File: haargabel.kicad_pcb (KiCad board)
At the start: 4 copper layers, 140 x 50 mm, 84 parts, among them J1 SWD, J2 USB_B_Micro, J3 Conn_01x02, SW1 SW_Push, U1 ATSAML21E15B-MUT, U2 MCP73831-2-OT, U3 TPS79330-EP, U4 TPS22929D, U5 MPU-6050

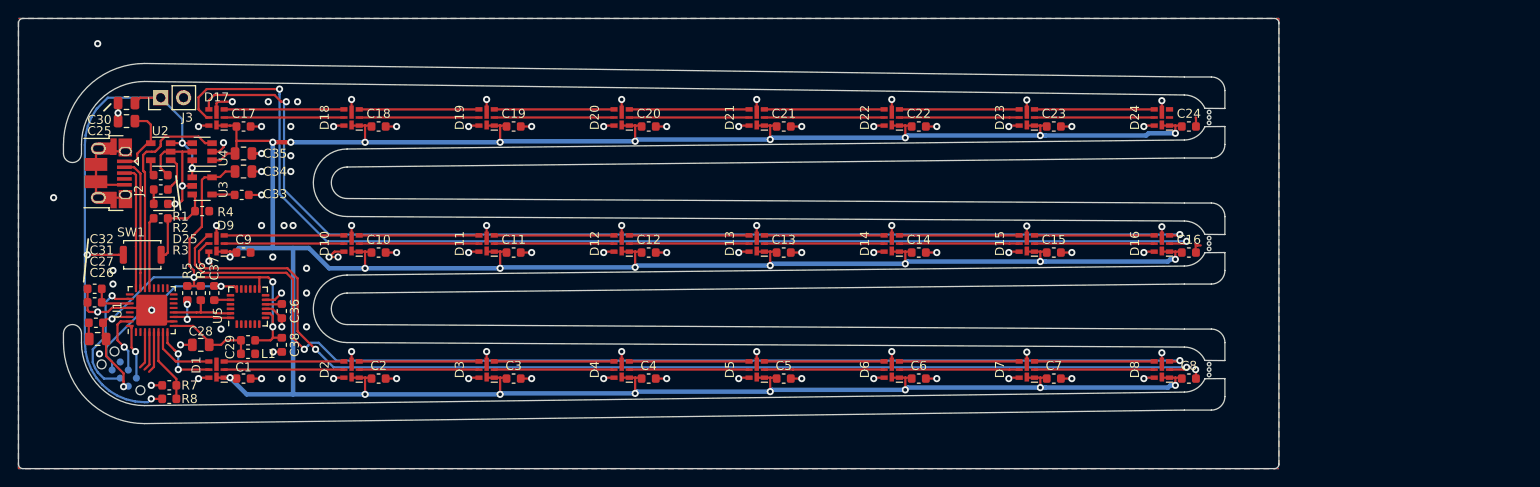
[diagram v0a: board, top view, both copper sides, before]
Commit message: Fix startup circuit
Use a zener-diode instead of just resistors.
This makes stuff much easier since it 'protects' the CPU from the high battery voltage.
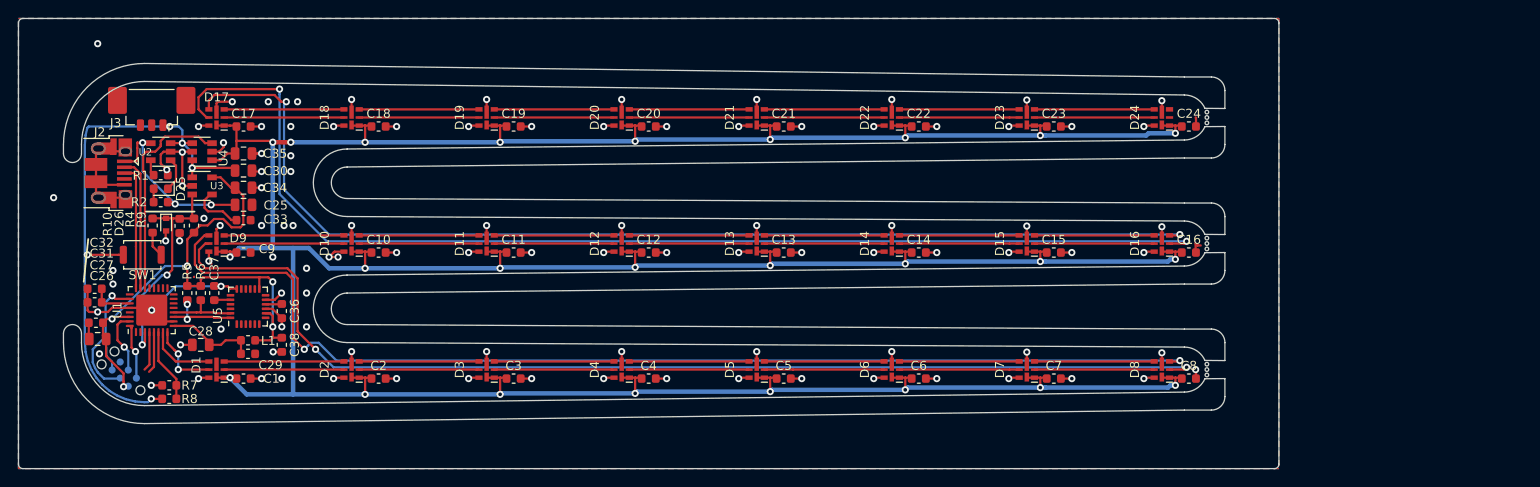
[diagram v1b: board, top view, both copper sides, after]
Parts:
- removed R3: 470R, Resistor_SMD:R_0603_1608Metric
- added D26: BZT52C2V7T-7, Diode_SMD:D_SOD-523, F.Cu at (119.4, 65.9)
- added R10: 270R, Resistor_SMD:R_0603_1608Metric, F.Cu at (117.9, 66.0)
- added R9: 270, Resistor_SMD:R_0603_1608Metric, F.Cu at (122.5, 66.0)
- J3: value Conn_01x02 -> Conn_01x03; footprint Connector_PinHeader_2.54mm:PinHeader_1x02_P2.54mm_Vertical -> Connector_Molex:Molex_PicoBlade_53398-0371_1x03-1MP_P1.25mm_Vertical
- R4: value 100k -> 1k
- moved C25 16.0 mm to (128.0, 63.7), turned to 0 degrees
- moved C30 15.0 mm to (128.0, 59.9), turned to 180 degrees
- moved R4 2.99 mm to (120.9, 66.0), turned to 270 degrees
- moved C33 2.81 mm to (128.0, 65.4)
- moved J3 2.06 mm to (117.8, 53.6), turned to 180 degrees
- moved C34 1.80 mm to (128.0, 61.8)
- moved D25 1.69 mm to (118.8, 61.9)
- moved R2 1.40 mm to (118.8, 63.4)
- moved H1 0.25 mm to (235.0, 68.0)
- moved H2 0.25 mm to (235.0, 82.0)
- moved H3 0.25 mm to (235.0, 54.0)
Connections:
- D25 pad 1: GND -> /STAT
- J3 pad 2: GND -> Net-(J3-Pad2)
- R2 pad 2: /STAT -> VBUS
- R4 pad 1: Net-(R3-Pad1) -> /EN
- SW1 pad 1: Net-(R3-Pad1) -> Net-(R10-Pad1)
- U1 pad 21: /PWR_ON -> Net-(U1-Pad21)
- U1 pad 3: Net-(U1-Pad3) -> /EN
- U3 pad 3: Net-(R3-Pad1) -> /EN
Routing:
- net /EN: track 0.00 -> 24.5 mm, vias 0 -> 2
- net VBUS: track 8.22 -> 21.1 mm, vias 0 -> 3
- net GND: track 198.2 -> 188.0 mm, vias 104 -> 107
- net Net-(R3-Pad1): track 9.98 -> 0.00 mm
- net /PWR_ON: track 7.95 -> 0.00 mm
- net +3V0: track 62.7 -> 67.0 mm
- net Net-(U1-Pad3): track 4.14 -> 0.00 mm
- net Net-(C33-Pad2): track 2.53 -> 6.06 mm
- net Net-(R10-Pad1): track 0.00 -> 2.86 mm
- net +BATT: track 67.5 -> 66.3 mm, vias 4 -> 5
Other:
- board text added: "r01"

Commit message: Remove the DIY-Panel, make it more pointy
The Fab will fuck up the routing anyway. Lets just hope they place the tabs somewhat reasonable.
The round ends were not pointy enough, fix them.
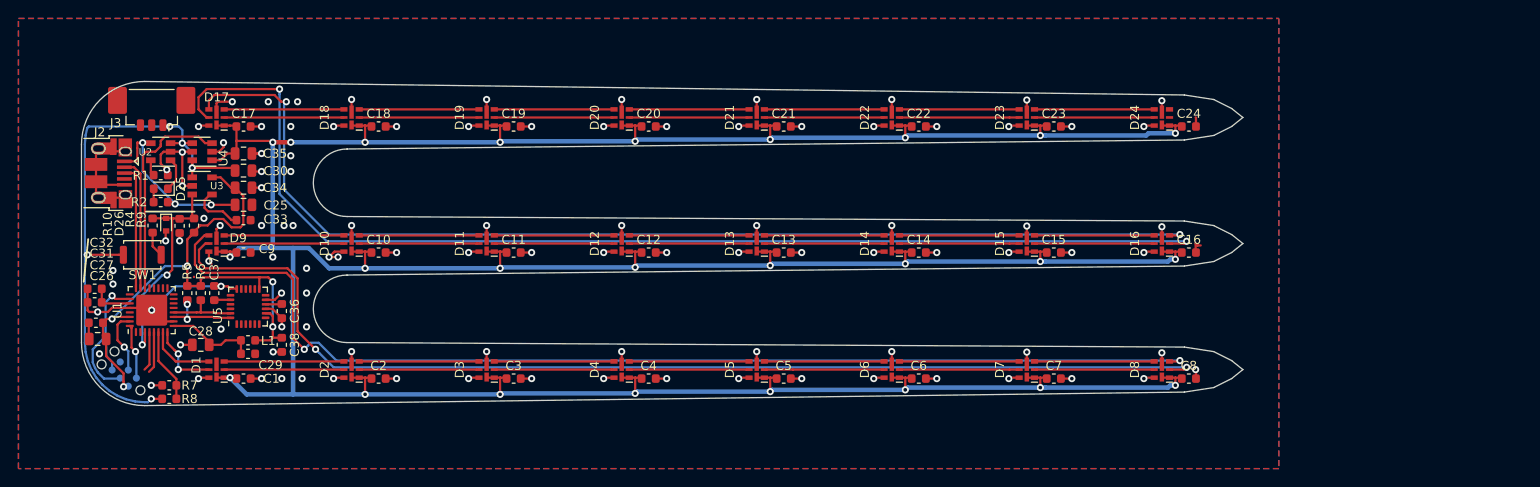
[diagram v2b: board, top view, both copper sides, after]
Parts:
- removed H1, H2, H3: MountingHole, MountingHole:Mousebite_0.4_0.6
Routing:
- net GND: track 188.0 -> 163.9 mm, vias 107 -> 105
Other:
- board size 140 x 50 mm -> 129 x 36 mm

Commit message: Make it longer
Add two more LEDs, making the whole thing 30mm longer
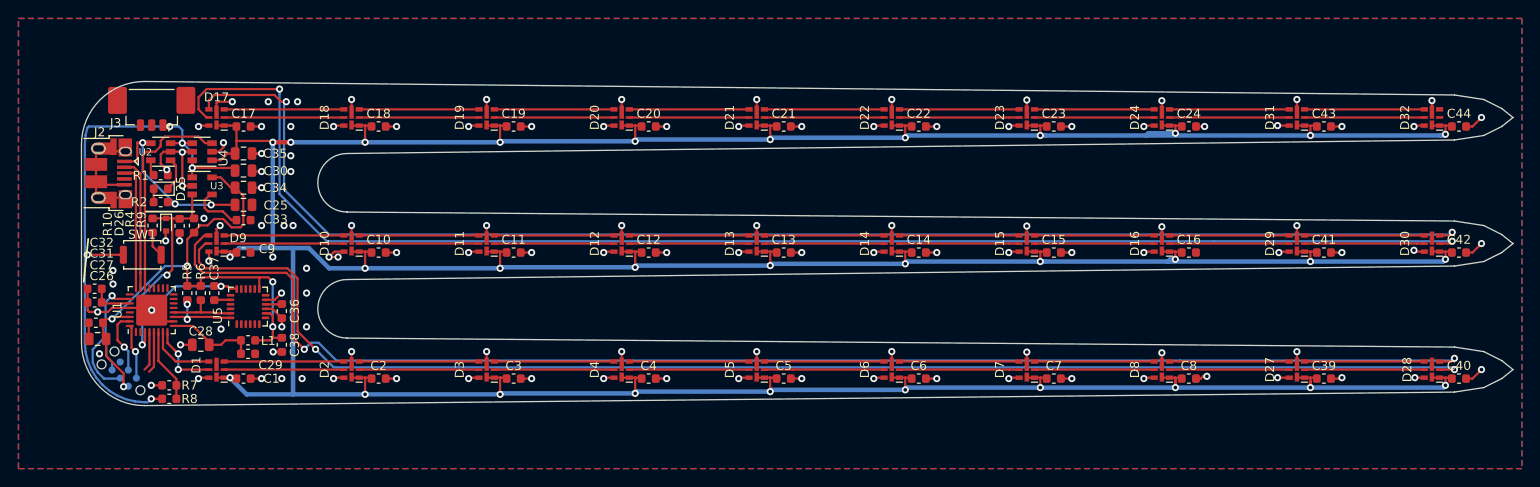
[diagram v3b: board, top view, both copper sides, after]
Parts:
- added C39: 100n, Capacitor_SMD:C_0603_1608Metric, F.Cu at (248.0, 83.0)
- added C40: 100n, Capacitor_SMD:C_0603_1608Metric, F.Cu at (263.0, 83.0)
- added C41: 100n, Capacitor_SMD:C_0603_1608Metric, F.Cu at (248.0, 69.0)
- added C42: 100n, Capacitor_SMD:C_0603_1608Metric, F.Cu at (263.0, 69.0)
- added C43: 100n, Capacitor_SMD:C_0603_1608Metric, F.Cu at (248.0, 55.0)
- added C44: 100n, Capacitor_SMD:C_0603_1608Metric, F.Cu at (263.0, 55.0)
- added D27: APA102-2020, LED_SMD:LED-APA102-2020, F.Cu at (245.0, 82.0)
- added D28: APA102-2020, LED_SMD:LED-APA102-2020, F.Cu at (260.0, 82.0)
- added D29: APA102-2020, LED_SMD:LED-APA102-2020, F.Cu at (245.0, 68.0)
- added D30: APA102-2020, LED_SMD:LED-APA102-2020, F.Cu at (260.0, 68.0)
- added D31: APA102-2020, LED_SMD:LED-APA102-2020, F.Cu at (245.0, 54.0)
- added D32: APA102-2020, LED_SMD:LED-APA102-2020, F.Cu at (260.0, 54.0)
- C1, C10, C11, C12, C13, C14, C15, C16, C17, C18, C19, C2, C20, C21, C22, C23, C24, C3, C4, C5, C6, C7, C8, C9: value C -> 100n
- R9: value 270 -> 270R
- SW1: value SW_Push -> SKRKAEE020
- turned SW1 to 0 degrees
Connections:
- D16 pad 2: /led8_3/CKI -> Net-(D16-Pad2)
- D16 pad 3: /led8_3/SDI -> Net-(D16-Pad3)
- D17 pad 4: /led8_3/SDI -> /led10_3/SDI
- D17 pad 5: /led8_3/CKI -> /led10_3/CKI
- D24 pad 2: /led8_3/CKO -> Net-(D24-Pad2)
- D24 pad 3: /led8_3/SDO -> Net-(D24-Pad3)
- D8 pad 2: /led8_2/CKI -> Net-(D27-Pad5)
- D8 pad 3: /led8_2/SDI -> Net-(D27-Pad4)
- D9 pad 4: /led8_2/SDI -> /led10_2/SDI
- D9 pad 5: /led8_2/CKI -> /led10_2/CKI
- SW1 pad 1: Net-(R10-Pad1) -> +BATT
- SW1 pad 2: +BATT -> Net-(R10-Pad1)
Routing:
- net /led10_3/CKI: track 0.00 -> 157.8 mm, vias 0 -> 2
- net /led10_2/SDI: track 0.00 -> 154.8 mm, vias 0 -> 2
- net /led10_3/SDI: track 0.00 -> 153.5 mm, vias 0 -> 2
- net /led10_2/CKI: track 0.00 -> 152.2 mm, vias 0 -> 2
- net /led8_3/CKI: track 128.8 -> 0.00 mm, vias 2 -> 0
- net /led8_2/SDI: track 123.6 -> 0.00 mm, vias 2 -> 0
- net /led8_3/SDI: track 122.8 -> 0.00 mm, vias 2 -> 0
- net /led8_2/CKI: track 122.7 -> 0.00 mm, vias 2 -> 0
- net VCC: track 437.3 -> 553.2 mm, vias 25 -> 31
- net GND: track 163.9 -> 185.4 mm, vias 105 -> 122
- net Net-(D27-Pad5): track 0.00 -> 13.3 mm
- net Net-(D27-Pad4): track 0.00 -> 13.3 mm
- net Net-(D24-Pad3): track 0.00 -> 13.3 mm
- net Net-(D24-Pad2): track 0.00 -> 13.3 mm
- net Net-(D16-Pad3): track 0.00 -> 13.3 mm
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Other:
- board size 129 x 36 mm -> 159 x 36 mm

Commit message: Re-Annotate, so the LED numbering makes more sense
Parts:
- renumbered C25 to C1, C34 to C10, C36 to C11, C37 to C12, C38 to C13, C35 to C14, C1 to C15, C2 to C16, C3 to C17, C4 to C18, C5 to C19, C26 to C2, C6 to C20, C7 to C21, C8 to C22, C39 to C23, C40 to C24, C9 to C25, C10 to C26, C11 to C27, C12 to C28, C13 to C29, C27 to C3, C14 to C30, C15 to C31, C16 to C32, C41 to C33, C42 to C34, C17 to C35, C18 to C36, C19 to C37, C20 to C38, C21 to C39, C28 to C4, C22 to C40, C23 to C41, C24 to C42, C30 to C5, C29 to C6, C31 to C7, C32 to C8, C33 to C9, D25 to D1, D8 to D10, D27 to D11, D28 to D12, D9 to D13, D10 to D14, D11 to D15, D12 to D16, D13 to D17, D14 to D18, D15 to D19, D26 to D2, D16 to D20, D29 to D21, D30 to D22, D17 to D23, D18 to D24, D19 to D25, D20 to D26, D21 to D27, D22 to D28, D23 to D29, D1 to D3, D24 to D30, D2 to D4, D3 to D5, D4 to D6, D5 to D7, D6 to D8, D7 to D9, R7 to R1, R8 to R2, R1 to R3, R2 to R4, R9 to R5, R4 to R6, R10 to R7, R5 to R8, R6 to R9, U5 to U4, U4 to U5
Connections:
- D32 pad 2: /led10_3/CKO -> (no net)
- D32 pad 3: /led10_3/SDO -> (no net)
- J1 pad 6: Net-(J1-Pad6) -> (no net)
- J2 pad 4: Net-(J2-Pad4) -> (no net)
- J3 pad 2: Net-(J3-Pad2) -> (no net)
- U1 pad 1: Net-(U1-Pad1) -> (no net)
- U1 pad 13: Net-(U1-Pad13) -> (no net)
- U1 pad 14: Net-(U1-Pad14) -> (no net)
- U1 pad 15: Net-(U1-Pad15) -> (no net)
- U1 pad 16: Net-(U1-Pad16) -> (no net)
- U1 pad 17: Net-(U1-Pad17) -> (no net)
- U1 pad 18: Net-(U1-Pad18) -> (no net)
- U1 pad 19: Net-(U1-Pad19) -> (no net)
- U1 pad 2: Net-(U1-Pad2) -> (no net)
- U1 pad 20: Net-(U1-Pad20) -> (no net)
- U1 pad 21: Net-(U1-Pad21) -> (no net)
- U1 pad 25: Net-(U1-Pad25) -> (no net)
- U1 pad 29: Net-(U1-Pad29) -> (no net)
- U1 pad 4: Net-(U1-Pad4) -> (no net)
- U1 pad 5: Net-(U1-Pad5) -> (no net)
- U4 pad 12: Net-(U5-Pad12) -> (no net)
- U4 pad 6: Net-(U5-Pad6) -> (no net)
- U4 pad 7: Net-(U5-Pad7) -> (no net)
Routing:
- net (no net): track 0.00 -> 9.03 mm
- net Net-(U1-Pad5): track 4.64 -> 0.00 mm
- net Net-(U1-Pad4): track 4.39 -> 0.00 mm
